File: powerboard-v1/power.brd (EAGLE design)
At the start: 139 x 70 mm, 42 parts, among them IC1 IR4428S, IC2 AD7887ARZ, IC3 ADUM2401ARWZ, IC4 78L05SMD, IC5 7812, Q1 IRF1018E, Q2 IRF1018E

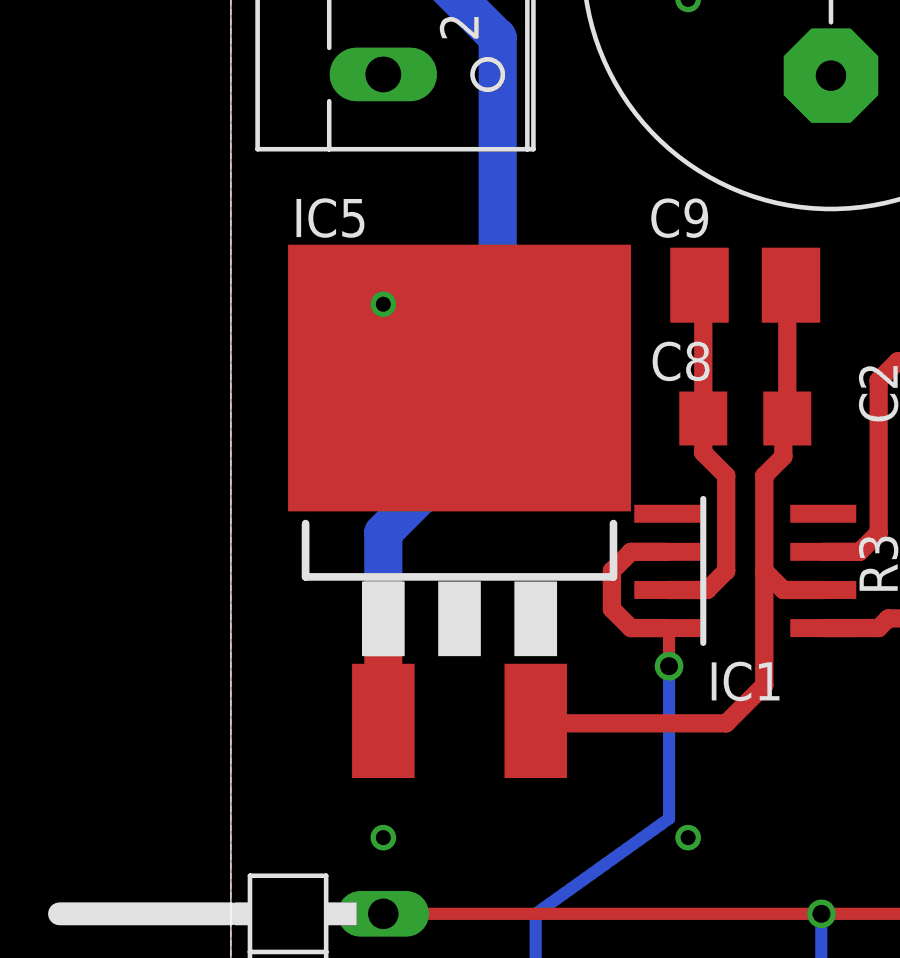
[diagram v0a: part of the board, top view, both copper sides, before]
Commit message: Fix clearance issues.
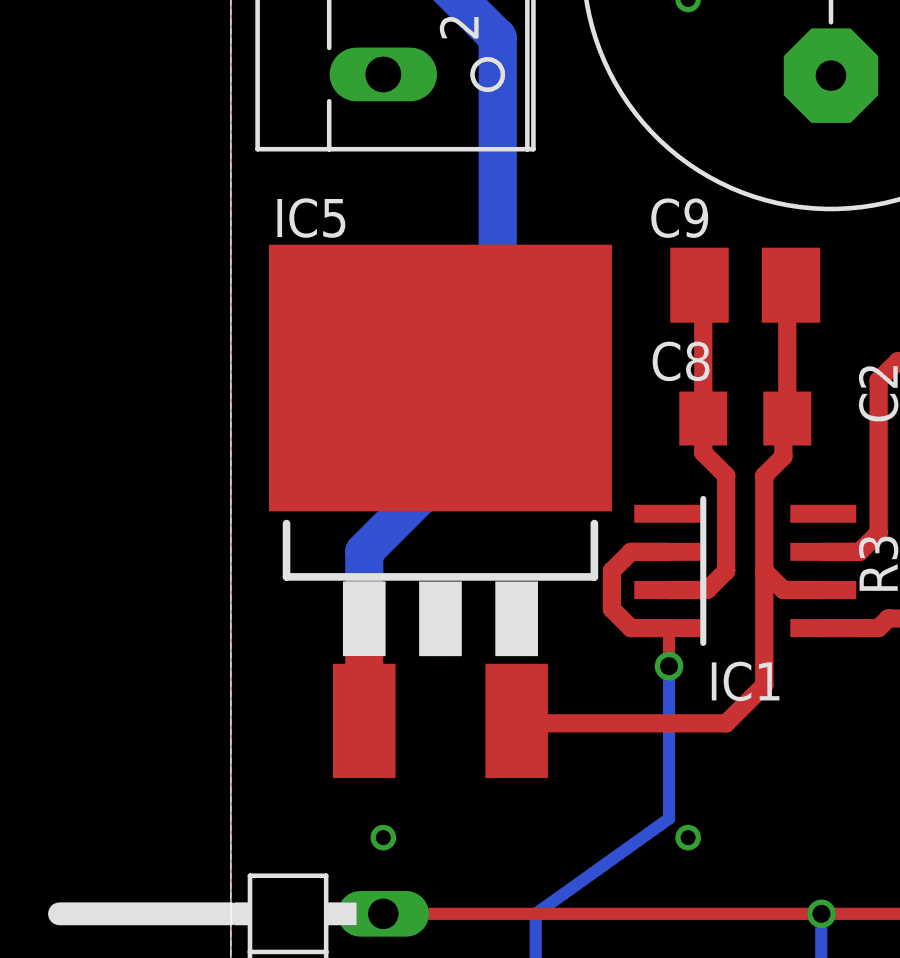
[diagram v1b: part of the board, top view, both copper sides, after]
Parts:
- moved IC5 0.63 mm to (6.99, 40.7)
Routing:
- net +12V: track 24.1 -> 24.7 mm
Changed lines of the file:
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@@
 <layer number="21" name="tPlace" color="7" fill="1" visible="yes" active="yes"/>
 <layer number="22" name="bPlace" color="7" fill="1" visible="yes" active="yes"/>
-<layer number="23" name="tOrigins" color="15" fill="1" visible="no" active="yes"/>
-<layer number="24" name="bOrigins" color="15" fill="1" visible="no" active="yes"/>
+<layer number="23" name="tOrigins" color="15" fill="1" visible="yes" active="yes"/>
+<layer number="24" name="bOrigins" color="15" fill="1" visible="yes" active="yes"/>
 <layer number="25" name="tNames" color="7" fill="1" visible="yes" active="yes"/>
 <layer number="26" name="bNames" color="7" fill="1" visible="yes" active="yes"/>
@@
 <layer number="46" name="Milling" color="3" fill="1" visible="yes" active="yes"/>
 <layer number="47" name="Measures" color="7" fill="1" visible="no" active="yes"/>
-<layer number="48" name="Document" color="7" fill="1" visible="no" active="yes"/>
-<layer number="49" name="Reference" color="7" fill="1" visible="no" active="yes"/>
-<layer number="51" name="tDocu" color="7" fill="1" visible="no" active="yes"/>
-<layer number="52" name="bDocu" color="7" fill="1" visible="no" active="yes"/>
+<layer number="48" name="Document" color="7" fill="1" visible="yes" active="yes"/>
+<layer number="49" name="Reference" color="7" fill="1" visible="yes" active="yes"/>
+<layer number="51" name="tDocu" color="7" fill="1" visible="yes" active="yes"/>
+<layer number="52" name="bDocu" color="7" fill="1" visible="yes" active="yes"/>
 <layer number="90" name="Modules" color="5" fill="1" visible="no" active="no"/>
 <layer number="91" name="Nets" color="2" fill="1" visible="no" active="no"/>
@@
 </element>
 <element name="IC3" library="local" package="SO-16W" value="ADUM2401ARWZ" x="92.63" y="11.43" rot="R270"/>
-<element name="IC5" library="local" package="D2PACK" value="7812" x="7.62" y="40.72"/>
+<element name="IC5" library="local" package="D2PACK" value="7812" x="6.985" y="40.72"/>
 <element name="JP1" library="pinhead" package="1X07/90" value="" x="1.27" y="17.78" rot="R90"/>
 <element name="Q1" library="local" package="TO220BV" value="IRF1018E" x="52.07" y="49.53" rot="R90"/>
@@
 <wire x1="16.51" y1="31.75" x2="17.78" y2="33.02" width="0.6096" layer="1"/>
 <wire x1="17.78" y1="33.02" x2="17.78" y2="36.83" width="0.6096" layer="1"/>
-<wire x1="10.24" y1="31.75" x2="10.16" y2="31.83" width="0.6096" layer="1"/>
+<wire x1="10.24" y1="31.75" x2="9.525" y2="31.83" width="0.6096" layer="1"/>
 </signal>
 <signal name="N$16">
@@
 <wire x1="38.1" y1="60.96" x2="45.72" y2="60.96" width="2.54" layer="1"/>
 <wire x1="45.72" y1="60.96" x2="50.8" y2="55.88" width="2.54" layer="1"/>
-<via x="5.08" y="35.56" extent="1-16" drill="0.6"/>
-<wire x1="5.08" y1="35.56" x2="5.08" y2="31.83" width="1.27" layer="1"/>
+<via x="4.445" y="35.56" extent="1-16" drill="0.6"/>
+<wire x1="4.445" y1="35.56" x2="4.445" y2="31.83" width="1.27" layer="1"/>
 <wire x1="5.08" y1="58.38" x2="5.12" y2="58.38" width="1.27" layer="16"/>
 <wire x1="5.12" y1="58.38" x2="8.89" y2="54.61" width="1.27" layer="16"/>
 <wire x1="8.89" y1="54.61" x2="8.89" y2="41.91" width="1.27" layer="16"/>
-<wire x1="8.89" y1="41.91" x2="5.08" y2="38.1" width="1.27" layer="16"/>
-<wire x1="5.08" y1="38.1" x2="5.08" y2="35.56" width="1.27" layer="16"/>
+<wire x1="8.89" y1="41.91" x2="4.445" y2="37.465" width="1.27" layer="16"/>
+<wire x1="4.445" y1="37.465" x2="4.445" y2="35.56" width="1.27" layer="16"/>
 <wire x1="51.7525" y1="40.77" x2="51.7525" y2="49.2125" width="1.27" layer="1"/>
 <wire x1="51.7525" y1="49.2125" x2="52.07" y2="49.53" width="1.27" layer="1"/>
@@
 <via x="66.04" y="45.72" extent="1-16" drill="0.5"/>
 </signal>
-<signal name="N$52">
-<via x="5.08" y="45.72" extent="1-16" drill="0.5"/>
-</signal>
 <signal name="N$53">

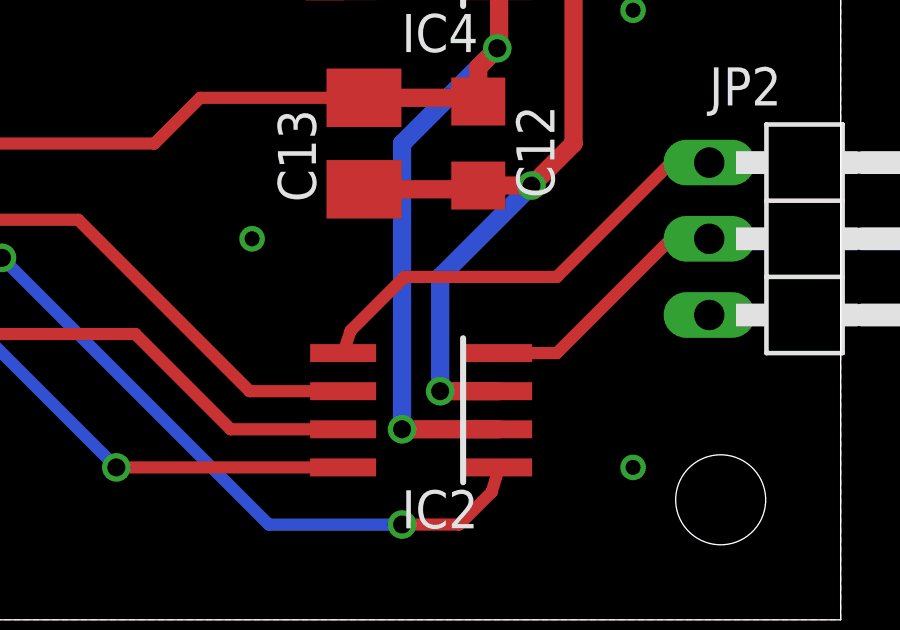
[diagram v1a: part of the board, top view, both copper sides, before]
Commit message: Fix a mislabeled pin.
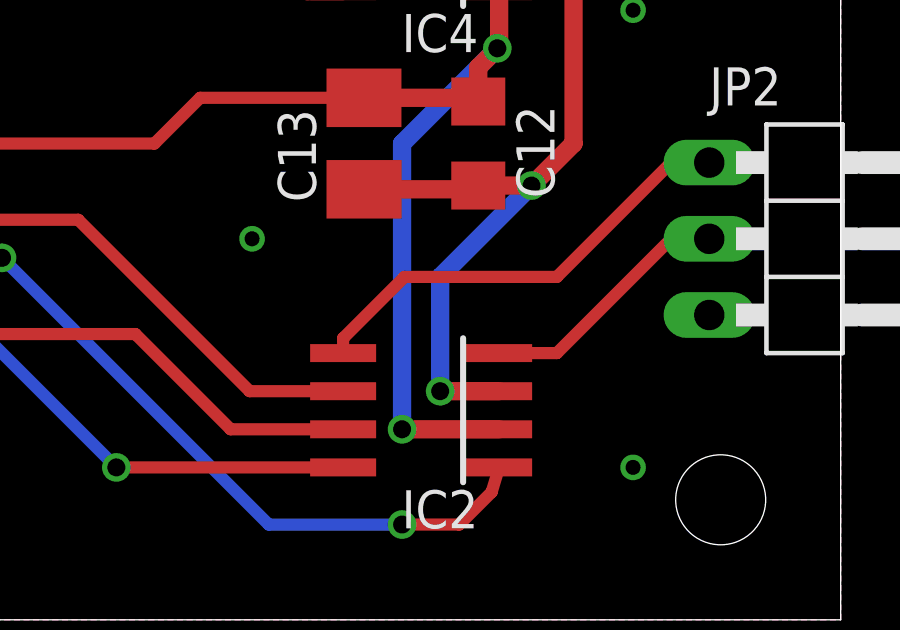
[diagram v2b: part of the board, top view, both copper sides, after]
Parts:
- IC2: device local:SO08 -> 50w-modular-psu:SO08
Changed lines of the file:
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@@
 <setting verticaltext="up"/>
 </settings>
-<grid distance="0.1" unitdist="inch" unit="inch" style="lines" multiple="1" display="no" altdistance="0.025" altunitdist="inch" altunit="inch"/>
+<grid distance="0.025" unitdist="inch" unit="inch" style="lines" multiple="1" display="no" altdistance="0.025" altunitdist="inch" altunit="inch"/>
 <layers>
 <layer number="1" name="Top" color="4" fill="1" visible="yes" active="yes"/>
@@
 <attribute name="VALUE" x="15.24" y="32.893" size="1.27" layer="27"/>
 </element>
-<element name="IC2" library="local" package="SO08" value="AD7887ARZ" x="125.015" y="6.985" smashed="yes" rot="R90">
+<element name="IC2" library="50w-modular-psu" package="SO08" value="AD7887ARZ" x="125.015" y="6.985" smashed="yes" rot="R90">
 <attribute name="NAME" x="126.92" y="4.318" size="1.27" layer="25" rot="R180"/>
 <attribute name="VALUE" x="126.92" y="10.922" size="1.27" layer="27" rot="R180"/>
@@
 <contactref element="IC2" pad="4"/>
 <contactref element="JP2" pad="2"/>
-<wire x1="127.615" y1="8.89" x2="129.54" y2="8.89" width="0.4064" layer="1"/>
 <wire x1="129.54" y1="8.89" x2="133.35" y2="12.7" width="0.4064" layer="1"/>
 <wire x1="133.35" y1="12.7" x2="134.62" y2="12.7" width="0.4064" layer="1"/>
+<wire x1="129.54" y1="8.89" x2="127.615" y2="8.89" width="0.4064" layer="1"/>
 </signal>
 <signal name="+12V">
@@
 <contactref element="IC2" pad="5"/>
 <contactref element="JP2" pad="1"/>
-<wire x1="122.415" y1="8.89" x2="122.665" y2="9.635" width="0.4064" layer="1"/>
-<wire x1="122.665" y1="9.635" x2="124.46" y2="11.43" width="0.4064" layer="1"/>
+<wire x1="122.415" y1="9.385" x2="124.46" y2="11.43" width="0.4064" layer="1"/>
 <wire x1="124.46" y1="11.43" x2="129.54" y2="11.43" width="0.4064" layer="1"/>
 <wire x1="129.54" y1="11.43" x2="133.35" y2="15.24" width="0.4064" layer="1"/>
 <wire x1="133.35" y1="15.24" x2="134.62" y2="15.24" width="0.4064" layer="1"/>
+<wire x1="122.415" y1="8.89" x2="122.415" y2="9.385" width="0.4064" layer="1"/>
 </signal>
 <signal name="N$18">

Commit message: D3: BAS70->BAS21.
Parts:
- D3: value BAS70 -> BAS21
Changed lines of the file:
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@@
 <attribute name="VALUE" x="51.435" y="27.305" size="1.27" layer="27" rot="R90"/>
 </element>
-<element name="D3" library="diode" package="SOT23" value="BAS70" x="118.665" y="26.67" smashed="yes" rot="R270">
+<element name="D3" library="diode" package="SOT23" value="BAS21" x="118.665" y="26.67" smashed="yes" rot="R270">
 <attribute name="NAME" x="117.395" y="24.765" size="1.27" layer="25" rot="R270"/>
 <attribute name="VALUE" x="115.49" y="28.575" size="1.27" layer="27" rot="R270"/>
